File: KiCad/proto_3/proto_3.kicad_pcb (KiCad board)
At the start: 2 copper layers, 12 parts

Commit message: Moving folders around
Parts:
- renumbered D1 to TVS1
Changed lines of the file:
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@@
 	(net 2 "Net-(U1-+V(cap))")
 	(net 3 "Net-(U1-+Vo)")
-	(net 4 "Net-(D1-A2)")
-	(net 5 "Net-(FUSE1-Pad2)")
-	(net 6 "Net-(U1-AC(L))")
-	(net 7 "Net-(LDM1-Pad2)")
-	(net 8 "Net-(D1-A1)")
-	(net 9 "Net-(FUSE1-Pad1)")
-	(net 10 "Net-(U1-AC(N))")
+	(net 4 "Net-(FUSE1-Pad2)")
+	(net 5 "Net-(U1-AC(L))")
+	(net 6 "Net-(LDM1-Pad2)")
+	(net 7 "Net-(FUSE1-Pad1)")
+	(net 8 "Net-(U1-AC(N))")
+	(net 9 "Net-(TVS1-A2)")
+	(net 10 "Net-(TVS1-A1)")
 	(footprint "Capacitor-470uF-16V:CAP_RHT_8X11P5_NCH"
 		(layer "F.Cu")
@@
 			(layers "*.Cu" "*.Mask")
 			(remove_unused_layers no)
-			(net 4 "Net-(D1-A2)")
+			(net 9 "Net-(TVS1-A2)")
 			(pintype "unspecified")
 		)
@@
 			(layers "*.Cu" "*.Mask")
 			(remove_unused_layers no)
-			(net 8 "Net-(D1-A1)")
+			(net 10 "Net-(TVS1-A1)")
 			(pinfunction "1")
 			(pintype "unspecified")
@@
 			(layers "*.Cu" "*.Mask")
 			(remove_unused_layers no)
-			(net 5 "Net-(FUSE1-Pad2)")
+			(net 4 "Net-(FUSE1-Pad2)")
 			(pintype "unspecified")
 		)
@@
 			(layers "*.Cu" "*.Mask")
 			(remove_unused_layers no)
-			(net 7 "Net-(LDM1-Pad2)")
+			(net 6 "Net-(LDM1-Pad2)")
 			(pintype "unspecified")
 		)
@@
 			(layers "*.Cu" "*.Mask")
 			(remove_unused_layers no)
-			(net 6 "Net-(U1-AC(L))")
+			(net 5 "Net-(U1-AC(L))")
 			(pinfunction "AC(L)")
 			(pintype "bidirectional")
@@
 			(layers "*.Cu" "*.Mask")
 			(remove_unused_layers no)
-			(net 10 "Net-(U1-AC(N))")
+			(net 8 "Net-(U1-AC(N))")
 			(pinfunction "AC(N)")
 			(pintype "bidirectional")
@@
 			(layers "*.Cu" "*.Mask")
 			(remove_unused_layers no)
-			(net 4 "Net-(D1-A2)")
+			(net 9 "Net-(TVS1-A2)")
 			(pinfunction "-Vo")
 			(pintype "bidirectional")
@@
 			(layers "*.Cu" "*.Mask")
 			(remove_unused_layers no)
-			(net 8 "Net-(D1-A1)")
+			(net 10 "Net-(TVS1-A1)")
 			(pintype "unspecified")
 		)
@@
 			(layers "*.Cu" "*.Mask")
 			(remove_unused_layers no)
-			(net 4 "Net-(D1-A2)")
+			(net 9 "Net-(TVS1-A2)")
 			(pintype "unspecified")
 		)
@@
 			(layers "*.Cu" "*.Mask")
 			(remove_unused_layers no)
-			(net 6 "Net-(U1-AC(L))")
+			(net 5 "Net-(U1-AC(L))")
 			(pinfunction "1")
 			(pintype "unspecified")
@@
 			(layers "*.Cu" "*.Mask")
 			(remove_unused_layers no)
-			(net 7 "Net-(LDM1-Pad2)")
+			(net 6 "Net-(LDM1-Pad2)")
 			(pinfunction "2")
 			(pintype "unspecified")
@@
 			(layers "*.Cu" "*.Mask")
 			(remove_unused_layers no)
-			(net 8 "Net-(D1-A1)")
+			(net 10 "Net-(TVS1-A1)")
 			(pintype "passive")
 			(solder_mask_margin 0.102)
@@
 			(layers "*.Cu" "*.Mask")
 			(remove_unused_layers no)
-			(net 4 "Net-(D1-A2)")
+			(net 9 "Net-(TVS1-A2)")
 			(pintype "passive")
 			(solder_mask_margin 0.102)
@@
 			(layers "*.Cu" "*.Mask")
 			(remove_unused_layers no)
-			(net 10 "Net-(U1-AC(N))")
+			(net 8 "Net-(U1-AC(N))")
 			(pintype "passive")
 			(solder_mask_margin 0.102)
@@
 			(layers "*.Cu" "*.Mask")
 			(remove_unused_layers no)
-			(net 9 "Net-(FUSE1-Pad1)")
+			(net 7 "Net-(FUSE1-Pad1)")
 			(pintype "passive")
 			(solder_mask_margin 0.102)
@@
 			(layers "*.Cu" "*.Mask")
 			(remove_unused_layers no)
-			(net 4 "Net-(D1-A2)")
+			(net 9 "Net-(TVS1-A2)")
 			(pintype "passive")
 			(solder_mask_margin 0.102)
@@
 			(layers "*.Cu" "*.Mask")
 			(remove_unused_layers no)
-			(net 9 "Net-(FUSE1-Pad1)")
+			(net 7 "Net-(FUSE1-Pad1)")
 			(pinfunction "1")
 			(pintype "unspecified")
@@
 			(layers "*.Cu" "*.Mask")
 			(remove_unused_layers no)
-			(net 5 "Net-(FUSE1-Pad2)")
+			(net 4 "Net-(FUSE1-Pad2)")
 			(pinfunction "2")
 			(pintype "unspecified")
@@
 			(layers "*.Cu" "*.Mask")
 			(remove_unused_layers no)
-			(net 8 "Net-(D1-A1)")
+			(net 10 "Net-(TVS1-A1)")
 			(pintype "unspecified")
 		)
@@
 			(layers "*.Cu" "*.Mask")
 			(remove_unused_layers no)
-			(net 4 "Net-(D1-A2)")
+			(net 9 "Net-(TVS1-A2)")
 			(pintype "unspecified")
 		)
@@
 		(descr "Diode SMB (DO-214AA)")
 		(tags "Diode SMB (DO-214AA)")
-		(property "Reference" "D1"
+		(property "Reference" "TVS1"
 			(at 0 -3 90)
 			(layer "F.SilkS")
@@
 			(size 2.1844 2.1844)
 			(layers "F.Cu" "F.Mask" "F.Paste")
-			(net 8 "Net-(D1-A1)")
+			(net 10 "Net-(TVS1-A1)")
 			(pinfunction "A1")
 			(pintype "passive")
@@
 			(size 2.1844 2.1844)
 			(layers "F.Cu" "F.Mask" "F.Paste")
-			(net 4 "Net-(D1-A2)")
+			(net 9 "Net-(TVS1-A2)")
 			(pinfunction "A2")
 			(pintype "passive")
@@
 	)
 	(segment
+		(start 149.000001 93)
+		(end 156 93)
+		(width 0.7814)
+		(layer "F.Cu")
+		(net 4)
+	)
+	(segment
+		(start 106 93)
+		(end 102 89)
+		(width 0.7814)
+		(layer "F.Cu")
+		(net 5)
+	)
+	(segment
+		(start 111.134 93)
+		(end 106 93)
+		(width 0.7814)
+		(layer "F.Cu")
+		(net 5)
+	)
+	(segment
+		(start 125 93)
+		(end 118.5 93)
+		(width 0.7814)
+		(layer "F.Cu")
+		(net 6)
+	)
+	(segment
+		(start 161.08 93)
+		(end 185 93)
+		(width 0.7814)
+		(layer "F.Cu")
+		(net 7)
+	)
+	(segment
+		(start 185 93)
+		(end 192 86)
+		(width 0.7814)
+		(layer "F.Cu")
+		(net 7)
+	)
+	(segment
+		(start 188 85)
+		(end 192 81)
+		(width 0.7814)
+		(layer "F.Cu")
+		(net 8)
+	)
+	(segment
+		(start 102 85)
+		(end 188 85)
+		(width 0.7814)
+		(layer "F.Cu")
+		(net 8)
+	)
+	(segment
 		(start 151 71.9892)
 		(end 151.9892 71.9892)
 		(width 0.7814)
 		(layer "F.Cu")
-		(net 4)
+		(net 9)
 	)
 	(segment
@@
 		(width 0.7814)
 		(layer "F.Cu")
-		(net 4)
+		(net 9)
 	)
 	(segment
@@
 		(width 0.7814)
 		(layer "F.Cu")
-		(net 4)
+		(net 9)
 	)
 	(segment
@@
 		(width 0.7814)
 		(layer "F.Cu")
-		(net 4)
+		(net 9)
 	)
 	(segment
@@
 		(width 0.7814)
 		(layer "F.Cu")
-		(net 4)
+		(net 9)
 	)
 	(segment
@@
 		(width 0.7814)
 		(layer "F.Cu")
-		(net 4)
+		(net 9)
 	)
 	(segment
@@
 		(width 0.7814)
 		(layer "F.Cu")
-		(net 4)
+		(net 9)
 	)
 	(segment
@@
 		(width 0.7814)
 		(layer "F.Cu")
-		(net 4)
+		(net 9)
 	)
 	(segment
@@
 		(width 0.7814)
 		(layer "F.Cu")
-		(net 4)
+		(net 9)
 	)
 	(segment
@@
 		(width 0.7814)
 		(layer "F.Cu")
-		(net 4)
+		(net 9)
 	)
 	(segment
@@
 		(width 0.7814)
 		(layer "F.Cu")
-		(net 4)
+		(net 9)
 	)
 	(segment
@@
 		(width 0.7814)
 		(layer "F.Cu")
-		(net 4)
-	)
-	(segment
-		(start 149.000001 93)
-		(end 156 93)
-		(width 0.7814)
-		(layer "F.Cu")
-		(net 5)
-	)
-	(segment
-		(start 106 93)
-		(end 102 89)
-		(width 0.7814)
-		(layer "F.Cu")
-		(net 6)
-	)
-	(segment
-		(start 111.134 93)
-		(end 106 93)
-		(width 0.7814)
-		(layer "F.Cu")
-		(net 6)
-	)
-	(segment
-		(start 125 93)
-		(end 118.5 93)
-		(width 0.7814)
-		(layer "F.Cu")
-		(net 7)
+		(net 9)
 	)
 	(segment
@@
 		(width 0.7814)
 		(layer "F.Cu")
-		(net 8)
+		(net 10)
 	)
 	(segment
@@
 		(width 0.7814)
 		(layer "F.Cu")
-		(net 8)
+		(net 10)
 	)
 	(segment
@@
 		(width 0.2)
 		(layer "F.Cu")
-		(net 8)
+		(net 10)
 	)
 	(segment
@@
 		(width 0.7814)
 		(layer "F.Cu")
-		(net 8)
+		(net 10)
 	)
 	(segment
@@
 		(width 0.7814)
 		(layer "F.Cu")
-		(net 8)
+		(net 10)
 	)
 	(segment
@@
 		(width 0.2)
 		(layer "F.Cu")
-		(net 8)
+		(net 10)
 	)
 	(segment
@@
 		(width 0.7814)
 		(layer "F.Cu")
-		(net 8)
+		(net 10)
 	)
 	(segment
@@
 		(width 0.7814)
 		(layer "F.Cu")
-		(net 8)
+		(net 10)
 	)
 	(segment
@@
 		(width 0.7814)
 		(layer "F.Cu")
-		(net 8)
+		(net 10)
 	)
 	(segment
@@
 		(width 0.7814)
 		(layer "F.Cu")
-		(net 8)
-	)
-	(segment
-		(start 161.08 93)
-		(end 185 93)
-		(width 0.7814)
-		(layer "F.Cu")
-		(net 9)
-	)
-	(segment
-		(start 185 93)
-		(end 192 86)
-		(width 0.7814)
-		(layer "F.Cu")
-		(net 9)
-	)
-	(segment
-		(start 188 85)
-		(end 192 81)
-		(width 0.7814)
-		(layer "F.Cu")
-		(net 10)
-	)
-	(segment
-		(start 102 85)
-		(end 188 85)
-		(width 0.7814)
-		(layer "F.Cu")

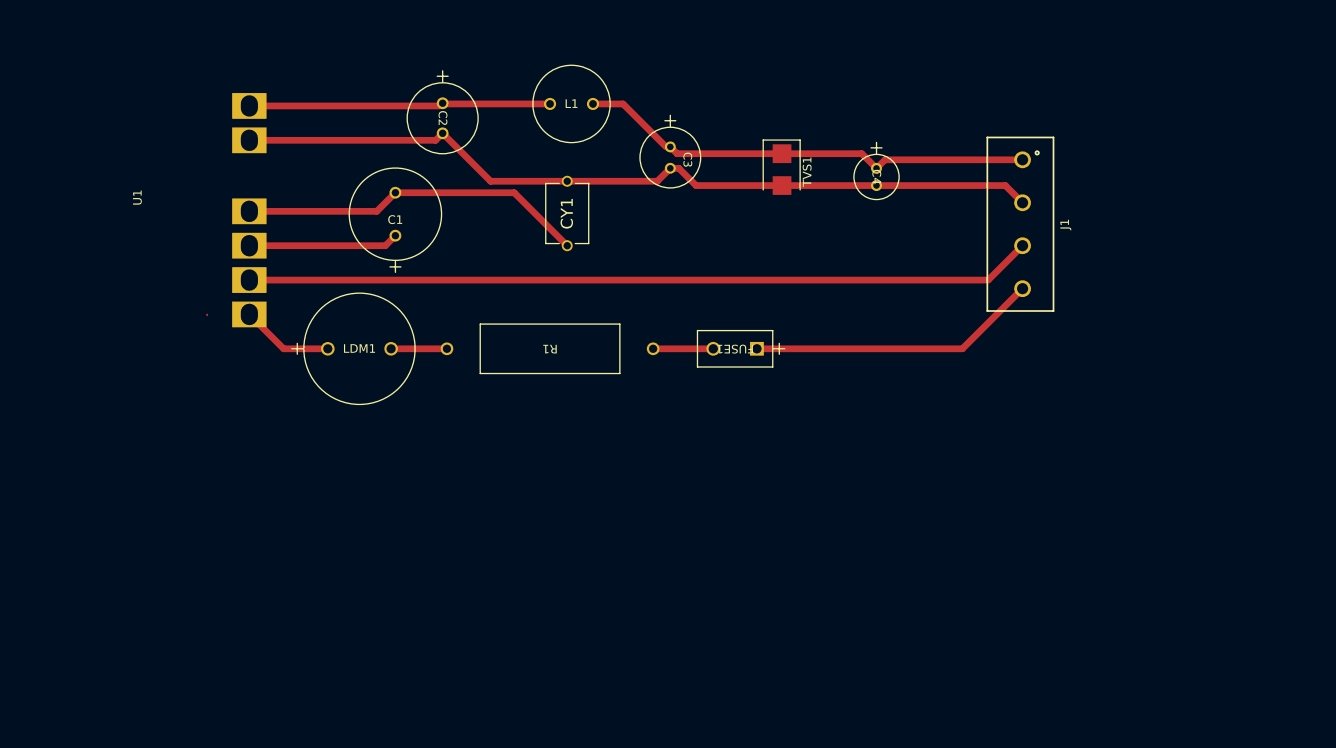
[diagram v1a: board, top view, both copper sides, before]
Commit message: Added mounting holes and ground pour
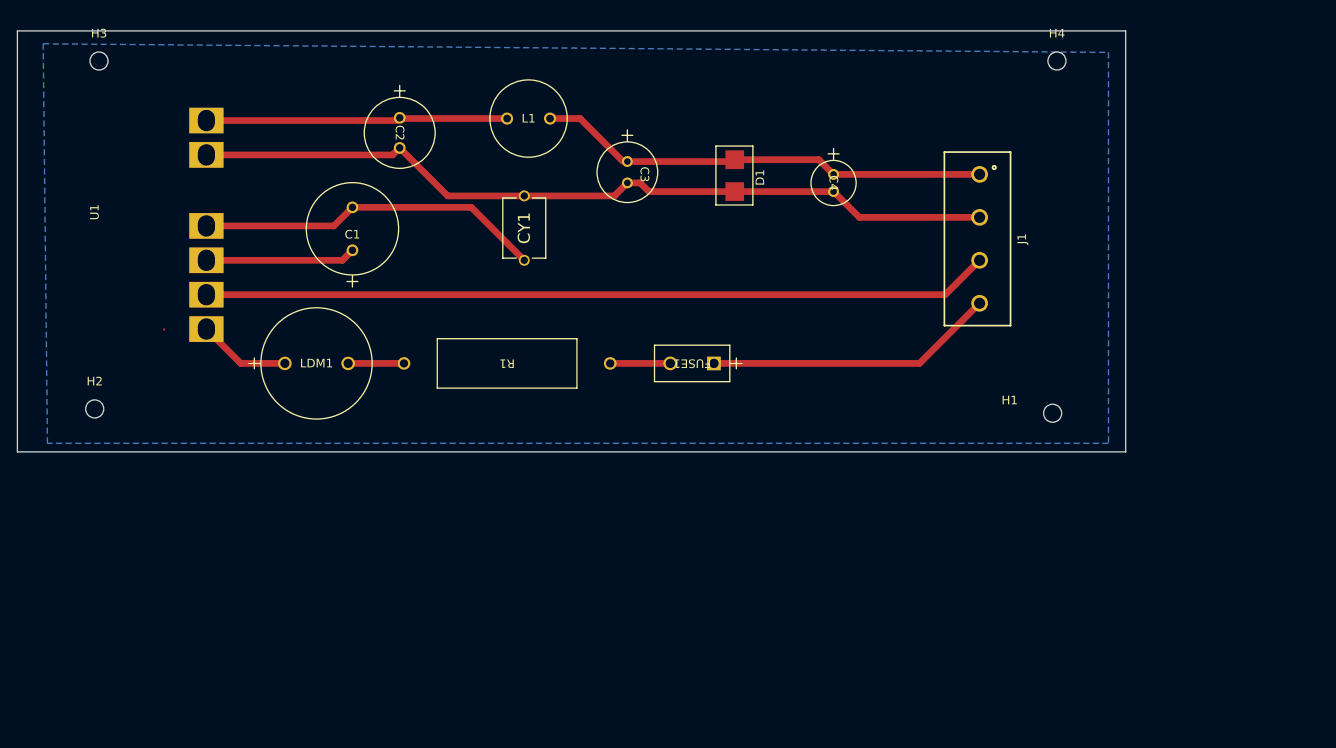
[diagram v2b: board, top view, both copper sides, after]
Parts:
- removed TVS1: SM6T6V8A, stuff:TVS_DIODE_NEW
- added D1: TVS, stuff:TVS_DIODE_NEW, F.Cu at (158.5, 73.1)
- added H1: MountingHole, MountingHole:MountingHole_2.1mm, F.Cu at (195.5, 100.5)
- added H2: MountingHole, MountingHole:MountingHole_2.1mm, F.Cu at (84.0, 100.0)
- added H3: MountingHole, MountingHole:MountingHole_2.1mm, F.Cu at (84.5, 59.5)
- added H4: MountingHole, MountingHole:MountingHole_2.1mm, F.Cu at (196.0, 59.5)
- moved C2 5.28 mm to (119.5, 66.1)
- moved C3 5.28 mm to (146.0, 71.2)
- moved CY1 5.28 mm to (134.0, 79.0)
- moved FUSE1 5.28 mm to (156.1, 94.7)
- moved J1 5.28 mm to (187.0, 80.2)
- moved L1 5.28 mm to (134.5, 66.2)
- moved LDM1 5.28 mm to (106.1, 94.7)
- moved R1 5.28 mm to (144.0, 94.7)
- moved C1 5.28 mm to (114.0, 81.5)
- moved U1 5.28 mm to (97.0, 77.1)
- moved C4 5.05 mm to (170.0, 72.7)
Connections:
- net Net-(FUSE1-Pad1) renamed GND
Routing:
- net Net-(D1-A1): track 53.8 -> 53.1 mm
- added copper zone on B.Cu, net GND
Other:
- board outline added: 129 x 49 mm

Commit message: seperated AC input and DC output, removed mounting holes
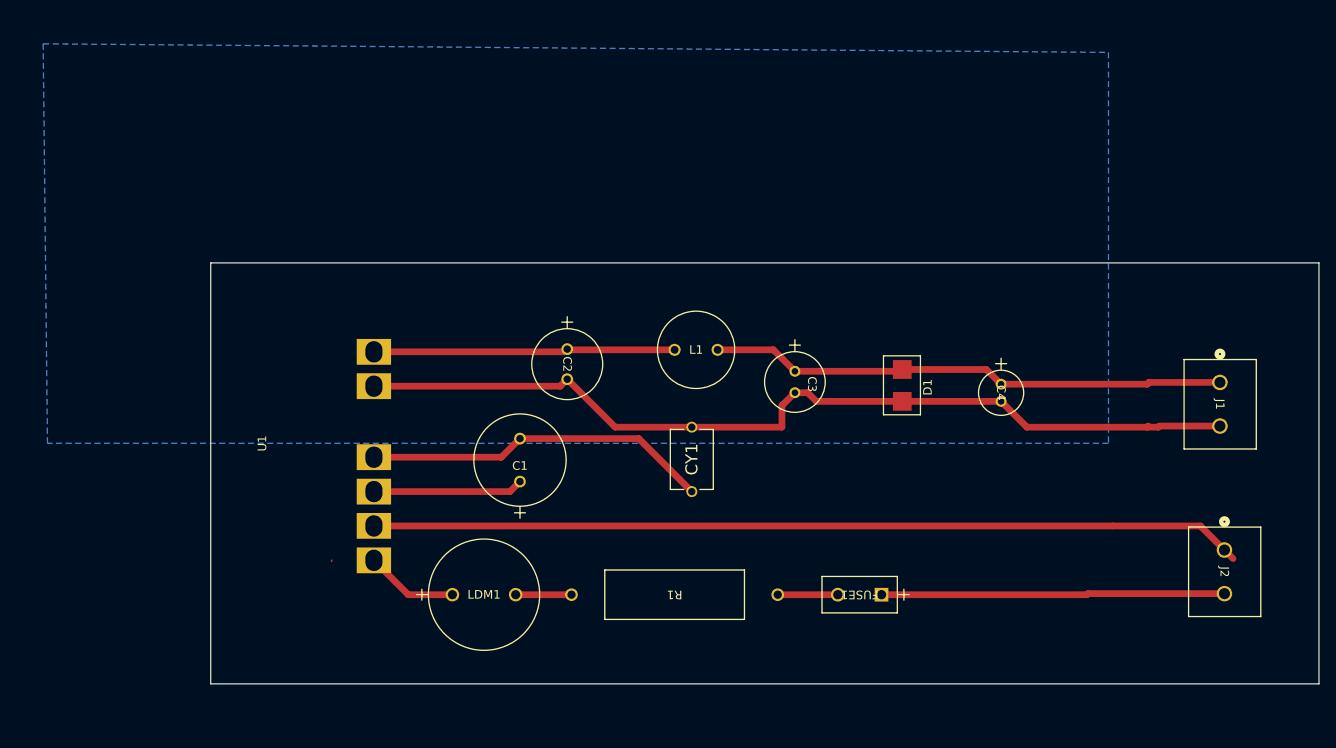
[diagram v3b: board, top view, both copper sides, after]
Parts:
- removed H1, H2, H3, H4: MountingHole, MountingHole:MountingHole_2.1mm
- added J2: 1729128, stuff:CONN_1729128_PXC, F.Cu at (215.5, 116.4)
- J1: value ~ -> 1729128; footprint stuff:screw_down_1x4 -> stuff:CONN_1729128_PXC
- moved C1 33.2 mm to (133.5, 108.5)
- moved C2 33.2 mm to (139.0, 93.0)
- moved CY1 33.2 mm to (153.5, 105.9)
- moved FUSE1 33.2 mm to (175.6, 121.6)
- moved L1 33.2 mm to (154.0, 93.1)
- moved LDM1 33.2 mm to (125.6, 121.6)
- moved R1 33.2 mm to (163.5, 121.6)
- moved U1 33.2 mm to (116.5, 104.0)
- moved J1 32.6 mm to (215.0, 96.9)
- moved C3 31.3 mm to (165.5, 95.6)
- moved C4 31.3 mm to (189.5, 97.1)
- moved D1 31.3 mm to (178.0, 97.5)
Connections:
- FUSE1 pad 1: GND -> Net-(FUSE1-Pad1)
- U1 pad 2: Net-(U1-AC(N)) -> GND
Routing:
- net Net-(U1-AC(N)): track 91.7 -> 0.00 mm
- net GND: track 33.8 -> 101.6 mm
- net Net-(FUSE1-Pad1): track 0.00 -> 40.0 mm
- net Net-(D1-A2): track 94.9 -> 106.1 mm
- net Net-(D1-A1): track 53.1 -> 61.1 mm

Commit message: Added power symbols, moved ground to output rail
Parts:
- moved C1 5.00 mm to (133.5, 113.5)
- moved C2 5.00 mm to (139.0, 98.0)
- moved C3 5.00 mm to (165.5, 100.6)
- moved C4 5.00 mm to (189.5, 102.1)
- moved CY1 5.00 mm to (153.5, 110.9)
- moved D1 5.00 mm to (178.0, 102.5)
- moved FUSE1 5.00 mm to (175.6, 126.6)
- moved J1 5.00 mm to (215.0, 101.9)
- moved J2 5.00 mm to (215.5, 121.4)
- moved L1 5.00 mm to (154.0, 98.1)
- moved LDM1 5.00 mm to (125.6, 126.6)
- moved R1 5.00 mm to (163.5, 126.6)
- moved U1 5.00 mm to (116.5, 109.0)
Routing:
- net (no net): track 0.10 -> 4.72 mm
